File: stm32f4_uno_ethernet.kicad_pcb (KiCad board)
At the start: 2 copper layers, 68.6 x 53.3 mm, 54 parts, among them J104 STM32 GPIO, J106 Power, J107 Ethernet, J110 Analog, J111 Conn_01x04, J201 RJ45-TH_B-1-1, U201 SRV05-4, U202 LAN8742A, Y201 25MHz

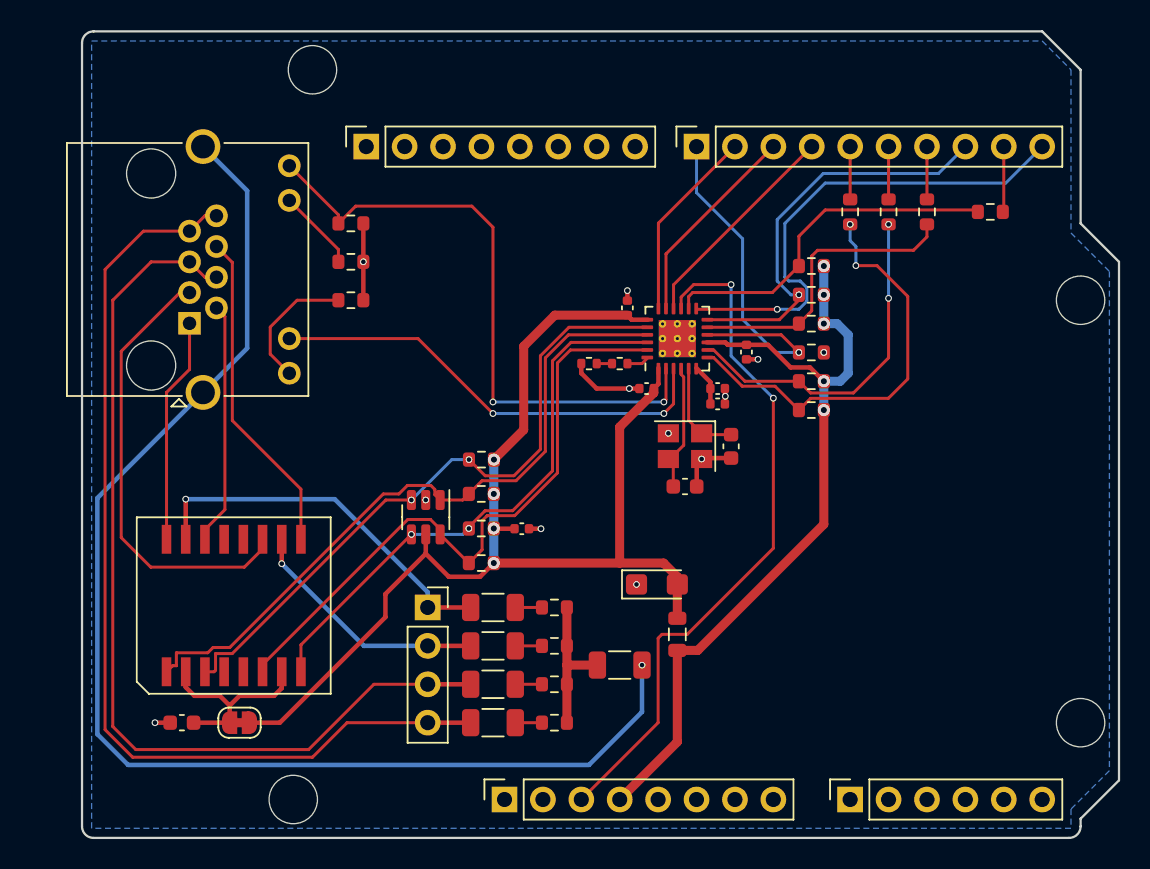
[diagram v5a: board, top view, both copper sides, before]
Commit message: Move PoE pin socket and add earth zone
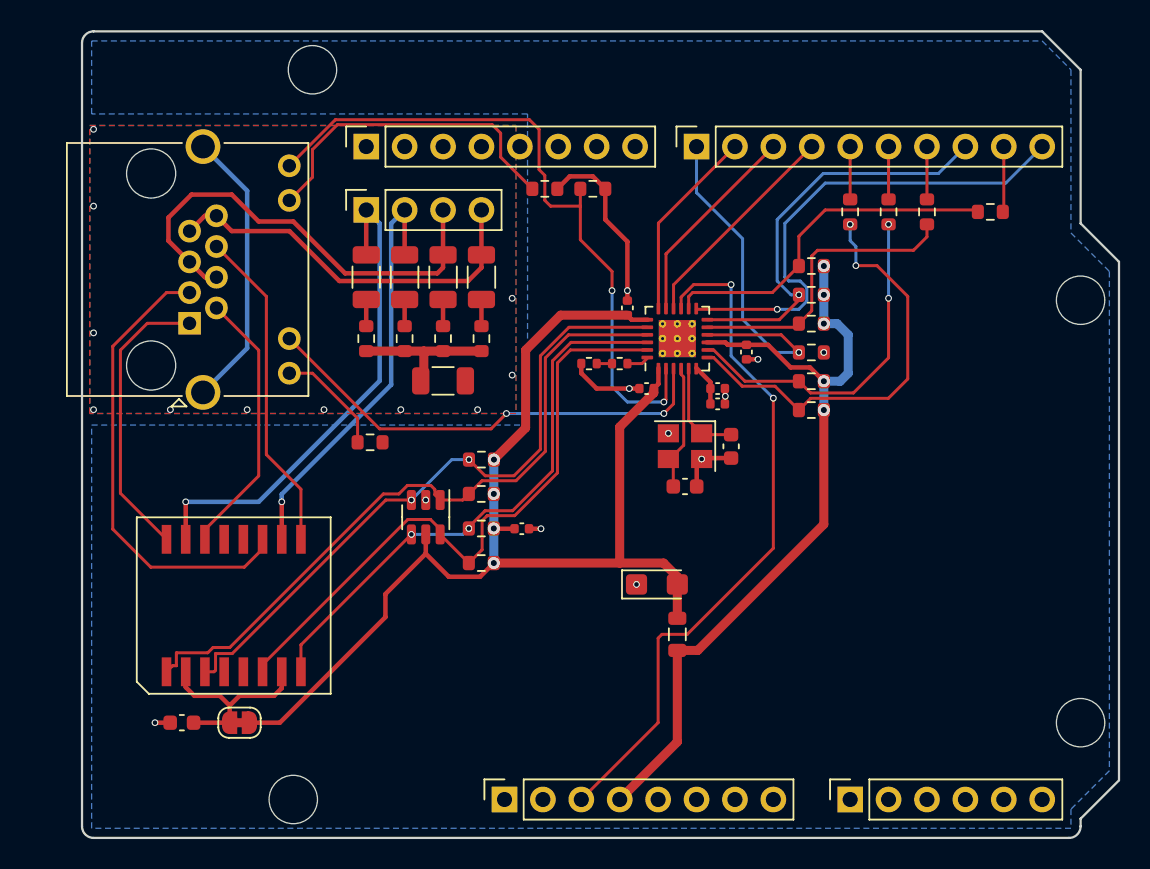
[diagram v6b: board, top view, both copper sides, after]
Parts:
- moved C214 29.5 mm to (126.4, 62.9), turned to -90 degrees
- moved C213 27.1 mm to (123.9, 62.9), turned to -90 degrees
- moved J111 26.6 mm to (118.8, 58.5), turned to 90 degrees
- moved R227 25.9 mm to (126.4, 67.0), turned to -90 degrees
- moved C212 25.1 mm to (121.3, 62.9), turned to -90 degrees
- moved R226 24.0 mm to (123.9, 67.0), turned to -90 degrees
- moved C211 23.4 mm to (118.8, 62.9), turned to -90 degrees
- moved R225 22.6 mm to (121.3, 67.0), turned to -90 degrees
- moved C215 22.1 mm to (123.9, 69.8)
- moved R224 21.7 mm to (118.8, 67.0), turned to -90 degrees
- moved R220 16.2 mm to (133.8, 57.1)
- moved R223 13.7 mm to (130.6, 57.1)
- moved R222 9.48 mm to (119.0, 73.8)
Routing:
- net Earth: track 85.6 -> 18.7 mm, vias 1 -> 11
- net /Ethernet/PR78: track 65.2 -> 25.7 mm
- net /Ethernet/PR45: track 62.6 -> 30.6 mm
- net /Ethernet/LED2_K: track 5.41 -> 21.9 mm
- net /Ethernet/PR36: track 16.4 -> 28.1 mm
- net /Ethernet/PR12: track 25.1 -> 33.3 mm
- net GND: track 18.2 -> 24.3 mm, vias 12 -> 11
- net /Ethernet/LAN1: track 14.9 -> 19.1 mm
- net /Ethernet/LED_speed: track 41.6 -> 45.5 mm
- net /Ethernet/LAN2: track 16.1 -> 17.9 mm
- net /Ethernet/LED1_K: track 8.82 -> 7.34 mm
- net /Ethernet/LAN3: track 29.7 -> 30.7 mm
- net /Ethernet/LED_link: track 30.1 -> 30.9 mm
- added copper zone on B.Cu, net Earth
- added copper zone on F.Cu, net Earth

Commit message: #2 Add silkscreen texts
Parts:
- added G***: LOGO, #Logo:e-Logo 5mm, F.Cu at (150.7, 80.8)
- moved R211 0.76 mm to (153.3, 59.4)
- moved R212 0.76 mm to (150.8, 59.4)
- moved R215 0.76 mm to (155.9, 59.4)
- moved R219 0.76 mm to (160.1, 59.4)
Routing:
- net /Ethernet/RXD1: track 28.2 -> 27.5 mm
- net /Ethernet/RXD0: track 23.0 -> 22.2 mm
- net /Ethernet/CRS_DV: track 20.0 -> 19.2 mm
- net /ETH_RXD1: track 3.49 -> 4.25 mm
- net /ETH_RXD0: track 3.49 -> 4.25 mm
- net /ETH_REF_CLK: track 4.34 -> 5.11 mm
- net /ETH_CRS_DV: track 3.49 -> 4.25 mm
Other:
- board text added: "+3V3"
- board text added: "+5V"
- board text added: "CRS DV"
- board text added: "GND"
- board text added: "MDC"
- board text added: "MDIO"
- board text added: "PR12"
- board text added: "PR36"
- board text added: "PR45"
- board text added: "PR78"
- board text added: "REF CLK"
- board text added: "RXD0"
- board text added: "RXD1"
- board text added: "RXER"
- board text added: "TX EN"
- board text added: "TXD0"
- board text added: "TXD1"
- board text added: "VBAT"
- board text added: "V_{IN}"
- board text added: "easy-smart.ch STM32F4 Uno Ethernet"
- board text added: "easy-smart.ch STM32F4 Uno Ethernet ${REVISION}"
- board text added: "~{RST}"

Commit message: Release 1.0.0 sent to JLCPCB
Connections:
- J104 pad 1: GND -> unconnected-(J104-Pin_1-Pad1)
- J104 pad 2: /PE14 -> unconnected-(J104-Pin_2-Pad2)
- J104 pad 3: /PE12 -> unconnected-(J104-Pin_3-Pad3)
- J104 pad 4: /PE10 -> unconnected-(J104-Pin_4-Pad4)
- J104 pad 5: /PE7 -> unconnected-(J104-Pin_5-Pad5)
- J104 pad 6: /PB2 -> unconnected-(J104-Pin_6-Pad6)
- J104 pad 7: /PB0 -> unconnected-(J104-Pin_7-Pad7)
- J104 pad 8: /PA3 -> unconnected-(J104-Pin_8-Pad8)
- J110 pad 1: /PE3 -> unconnected-(J110-Pin_1-Pad1)
- J110 pad 2: /PE5 -> unconnected-(J110-Pin_2-Pad2)
- J110 pad 3: /PC13 -> unconnected-(J110-Pin_3-Pad3)
- J110 pad 4: /PC2 -> unconnected-(J110-Pin_4-Pad4)
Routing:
- net GND: vias 11 -> 12
